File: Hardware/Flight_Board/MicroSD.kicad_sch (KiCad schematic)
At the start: 8 parts, among them J3 MEM2067-02-180-00-A_REVB

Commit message: clean up and finalize initial design
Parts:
- renumbered C19 to C25, C18 to C26, J3 to J5, R9 to R10, R7 to R11, R10 to R12, R6 to R9
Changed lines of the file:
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@@
   (symbol (lib_id "Device:R") (at 77.47 59.69 0) (unit 1)
     (in_bom yes) (on_board yes) (dnp no)
-    (property "Reference" "R10" (at 78.74 58.42 0)
+    (property "Reference" "R12" (at 78.74 58.42 0)
       (effects (font (size 1.27 1.27)) (justify left))
     )
@@
       (project "Flight_Board"
         (path "/e8eb85d5-f1ff-4500-895d-25b9ff5f6d36/d0c90712-c1df-4337-b369-5da6fbfa813f"
+          (reference "R12") (unit 1)
+        )
+      )
+    )
+  )
+  (symbol (lib_id "Device:R") (at 66.04 49.53 0) (unit 1)
+    (in_bom yes) (on_board yes) (dnp no)
+    (property "Reference" "R9" (at 67.31 48.26 0)
+      (effects (font (size 1.27 1.27)) (justify left))
+    )
+    (property "Value" "10k" (at 67.31 50.8 0)
+      (effects (font (size 1.27 1.27)) (justify left))
+    )
+    (property "Footprint" "" (at 64.262 49.53 90)
+      (effects (font (size 1.27 1.27)) hide)
+    )
+    (property "Datasheet" "~" (at 66.04 49.53 0)
+      (effects (font (size 1.27 1.27)) hide)
+    )
+    (pin "1")
+    (pin "2")
+    (instances
+      (project "Flight_Board"
+        (path "/e8eb85d5-f1ff-4500-895d-25b9ff5f6d36/d0c90712-c1df-4337-b369-5da6fbfa813f"
+          (reference "R9") (unit 1)
+        )
+      )
+    )
+  )
+  (symbol (lib_id "Device:R") (at 69.85 59.69 0) (unit 1)
+    (in_bom yes) (on_board yes) (dnp no)
+    (property "Reference" "R10" (at 71.12 58.42 0)
+      (effects (font (size 1.27 1.27)) (justify left))
+    )
+    (property "Value" "10k" (at 71.12 60.96 0)
+      (effects (font (size 1.27 1.27)) (justify left))
+    )
+    (property "Footprint" "" (at 68.072 59.69 90)
+      (effects (font (size 1.27 1.27)) hide)
+    )
+    (property "Datasheet" "~" (at 69.85 59.69 0)
+      (effects (font (size 1.27 1.27)) hide)
+    )
+    (pin "1")
+    (pin "2")
+    (instances
+      (project "Flight_Board"
+        (path "/e8eb85d5-f1ff-4500-895d-25b9ff5f6d36/d0c90712-c1df-4337-b369-5da6fbfa813f"
           (reference "R10") (unit 1)
         )
@@
     )
   )
-  (symbol (lib_id "Device:R") (at 66.04 49.53 0) (unit 1)
-    (in_bom yes) (on_board yes) (dnp no)
-    (property "Reference" "R6" (at 67.31 48.26 0)
-      (effects (font (size 1.27 1.27)) (justify left))
-    )
-    (property "Value" "10k" (at 67.31 50.8 0)
-      (effects (font (size 1.27 1.27)) (justify left))
-    )
-    (property "Footprint" "" (at 64.262 49.53 90)
-      (effects (font (size 1.27 1.27)) hide)
-    )
-    (property "Datasheet" "~" (at 66.04 49.53 0)
-      (effects (font (size 1.27 1.27)) hide)
-    )
-    (pin "1")
-    (pin "2")
-    (instances
-      (project "Flight_Board"
-        (path "/e8eb85d5-f1ff-4500-895d-25b9ff5f6d36/d0c90712-c1df-4337-b369-5da6fbfa813f"
-          (reference "R6") (unit 1)
-        )
-      )
-    )
-  )
-  (symbol (lib_id "Device:R") (at 69.85 59.69 0) (unit 1)
-    (in_bom yes) (on_board yes) (dnp no)
-    (property "Reference" "R9" (at 71.12 58.42 0)
-      (effects (font (size 1.27 1.27)) (justify left))
-    )
-    (property "Value" "10k" (at 71.12 60.96 0)
-      (effects (font (size 1.27 1.27)) (justify left))
-    )
-    (property "Footprint" "" (at 68.072 59.69 90)
-      (effects (font (size 1.27 1.27)) hide)
-    )
-    (property "Datasheet" "~" (at 69.85 59.69 0)
-      (effects (font (size 1.27 1.27)) hide)
-    )
-    (pin "1")
-    (pin "2")
-    (instances
-      (project "Flight_Board"
-        (path "/e8eb85d5-f1ff-4500-895d-25b9ff5f6d36/d0c90712-c1df-4337-b369-5da6fbfa813f"
-          (reference "R9") (unit 1)
-        )
-      )
-    )
-  )
   (symbol (lib_id "power:GND") (at 107.95 99.06 0) (unit 1)
     (in_bom yes) (on_board yes) (dnp no)
-    (property "Reference" "#PWR036" (at 107.95 105.41 0)
+    (property "Reference" "#PWR046" (at 107.95 105.41 0)
       (effects (font (size 1.27 1.27)) hide)
     )
@@
       (project "Flight_Board"
         (path "/e8eb85d5-f1ff-4500-895d-25b9ff5f6d36/d0c90712-c1df-4337-b369-5da6fbfa813f"
-          (reference "#PWR036") (unit 1)
+          (reference "#PWR046") (unit 1)
         )
       )
@@
   (symbol (lib_id "power:+3.3V") (at 88.9 41.91 0) (unit 1)
     (in_bom yes) (on_board yes) (dnp no) (fields_autoplaced)
-    (property "Reference" "#PWR035" (at 88.9 45.72 0)
+    (property "Reference" "#PWR043" (at 88.9 45.72 0)
       (effects (font (size 1.27 1.27)) hide)
     )
@@
       (project "Flight_Board"
         (path "/e8eb85d5-f1ff-4500-895d-25b9ff5f6d36/d0c90712-c1df-4337-b369-5da6fbfa813f"
-          (reference "#PWR035") (unit 1)
+          (reference "#PWR043") (unit 1)
         )
       )
@@
   (symbol (lib_id "Project:MEM2067-02-180-00-A_REVB") (at 115.57 76.2 0) (unit 1)
     (in_bom yes) (on_board yes) (dnp no) (fields_autoplaced)
-    (property "Reference" "J3" (at 132.08 80.01 0)
+    (property "Reference" "J5" (at 132.08 80.01 0)
       (effects (font (size 1.27 1.27)) (justify left))
     )
@@
       (project "Flight_Board"
         (path "/e8eb85d5-f1ff-4500-895d-25b9ff5f6d36/d0c90712-c1df-4337-b369-5da6fbfa813f"
-          (reference "J3") (unit 1)
+          (reference "J5") (unit 1)
         )
       )
@@
   (symbol (lib_id "Device:C") (at 99.06 45.72 0) (unit 1)
     (in_bom yes) (on_board yes) (dnp no)
-    (property "Reference" "C18" (at 101.6 44.45 0)
+    (property "Reference" "C26" (at 101.6 44.45 0)
       (effects (font (size 1.27 1.27)) (justify left))
     )
@@
       (project "Flight_Board"
         (path "/e8eb85d5-f1ff-4500-895d-25b9ff5f6d36/d0c90712-c1df-4337-b369-5da6fbfa813f"
-          (reference "C18") (unit 1)
+          (reference "C26") (unit 1)
         )
       )
@@
   (symbol (lib_id "power:GND") (at 99.06 49.53 0) (unit 1)
     (in_bom yes) (on_board yes) (dnp no)
-    (property "Reference" "#PWR037" (at 99.06 55.88 0)
+    (property "Reference" "#PWR045" (at 99.06 55.88 0)
       (effects (font (size 1.27 1.27)) hide)
     )
@@
       (project "Flight_Board"
         (path "/e8eb85d5-f1ff-4500-895d-25b9ff5f6d36/d0c90712-c1df-4337-b369-5da6fbfa813f"
-          (reference "#PWR037") (unit 1)
+          (reference "#PWR045") (unit 1)
         )
       )
@@
   (symbol (lib_id "Device:R") (at 73.66 49.53 0) (unit 1)
     (in_bom yes) (on_board yes) (dnp no)
-    (property "Reference" "R7" (at 74.93 48.26 0)
+    (property "Reference" "R11" (at 74.93 48.26 0)
       (effects (font (size 1.27 1.27)) (justify left))
     )
@@
       (project "Flight_Board"
         (path "/e8eb85d5-f1ff-4500-895d-25b9ff5f6d36/d0c90712-c1df-4337-b369-5da6fbfa813f"
-          (reference "R7") (unit 1)
+          (reference "R11") (unit 1)
         )
       )
@@
   (symbol (lib_id "power:GND") (at 88.9 49.53 0) (unit 1)
     (in_bom yes) (on_board yes) (dnp no)
-    (property "Reference" "#PWR038" (at 88.9 55.88 0)
+    (property "Reference" "#PWR044" (at 88.9 55.88 0)
       (effects (font (size 1.27 1.27)) hide)
     )
@@
       (project "Flight_Board"
         (path "/e8eb85d5-f1ff-4500-895d-25b9ff5f6d36/d0c90712-c1df-4337-b369-5da6fbfa813f"
-          (reference "#PWR038") (unit 1)
+          (reference "#PWR044") (unit 1)
         )
       )
@@
   (symbol (lib_id "Device:C") (at 88.9 45.72 0) (unit 1)
     (in_bom yes) (on_board yes) (dnp no)
-    (property "Reference" "C19" (at 91.44 44.45 0)
+    (property "Reference" "C25" (at 91.44 44.45 0)
       (effects (font (size 1.27 1.27)) (justify left))
     )
@@
       (project "Flight_Board"
         (path "/e8eb85d5-f1ff-4500-895d-25b9ff5f6d36/d0c90712-c1df-4337-b369-5da6fbfa813f"
-          (reference "C19") (unit 1)
-        )
-      )
+          (reference "C25") (unit 1)
+        )
+      )

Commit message: Added Mason's Feedback
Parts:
- added C33, C34, C35, C36: 22p, symbol Device:C
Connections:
- net GND: now also C33.2, C34.2, C35.2, C36.2
- net SDIO_D0: now also C36.1
- net SDIO_D1: now also C35.1
- net SDIO_D2: now also C34.1
- net SDIO_D3: now also C33.1
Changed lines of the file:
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@@
   (junction (at 99.06 41.91) (diameter 0) (color 0 0 0 0)
   )
-  (wire (pts (xy 110.49 76.2) (xy 66.04 76.2))
+  (wire (pts (xy 66.04 76.2) (xy 110.49 76.2))
     (stroke (width 0) (type default))
   )
@@
     (stroke (width 0) (type default))
   )
-  (wire (pts (xy 110.49 68.58) (xy 77.47 68.58))
+  (wire (pts (xy 73.66 71.12) (xy 73.66 82.55))
+    (stroke (width 0) (type default))
+  )
+  (wire (pts (xy 77.47 68.58) (xy 110.49 68.58))
     (stroke (width 0) (type default))
   )
@@
     (stroke (width 0) (type default))
   )
-  (wire (pts (xy 77.47 68.58) (xy 77.47 63.5))
-    (stroke (width 0) (type default))
-  )
   (wire (pts (xy 110.49 66.04) (xy 107.95 66.04))
     (stroke (width 0) (type default))
@@
     (stroke (width 0) (type default))
   )
+  (wire (pts (xy 77.47 68.58) (xy 77.47 86.36))
+    (stroke (width 0) (type default))
+  )
   (wire (pts (xy 110.49 88.9) (xy 107.95 88.9))
     (stroke (width 0) (type default))
@@
     (stroke (width 0) (type default))
   )
+  (wire (pts (xy 69.85 73.66) (xy 69.85 92.71))
+    (stroke (width 0) (type default))
+  )
   (wire (pts (xy 107.95 41.91) (xy 107.95 66.04))
     (stroke (width 0) (type default))
@@
     (stroke (width 0) (type default))
   )
+  (wire (pts (xy 66.04 76.2) (xy 66.04 86.36))
+    (stroke (width 0) (type default))
+  )
   (wire (pts (xy 107.95 96.52) (xy 107.95 99.06))
     (stroke (width 0) (type default))
@@
   )
   (wire (pts (xy 77.47 41.91) (xy 77.47 55.88))
+    (stroke (width 0) (type default))
+  )
+  (wire (pts (xy 77.47 63.5) (xy 77.47 68.58))
     (stroke (width 0) (type default))
   )
@@
         (path "/e8eb85d5-f1ff-4500-895d-25b9ff5f6d36/d0c90712-c1df-4337-b369-5da6fbfa813f"
           (reference "#PWR043") (unit 1)
+        )
+      )
+    )
+  )
+  (symbol (lib_id "Device:C") (at 73.66 86.36 0) (unit 1)
+    (in_bom yes) (on_board yes) (dnp no)
+    (property "Reference" "C35" (at 76.2 82.55 0)
+      (effects (font (size 1.27 1.27)) (justify left))
+    )
+    (property "Value" "22p" (at 77.47 85.09 0)
+      (effects (font (size 1.27 1.27)) (justify left))
+    )
+    (property "Footprint" "" (at 74.6252 90.17 0)
+      (effects (font (size 1.27 1.27)) hide)
+    )
+    (property "Datasheet" "~" (at 73.66 86.36 0)
+      (effects (font (size 1.27 1.27)) hide)
+    )
+    (pin "1")
+    (pin "2")
+    (instances
+      (project "Flight_Board"
+        (path "/e8eb85d5-f1ff-4500-895d-25b9ff5f6d36/d0c90712-c1df-4337-b369-5da6fbfa813f"
+          (reference "C35") (unit 1)
         )
       )
@@
     )
   )
+  (symbol (lib_id "power:GND") (at 77.47 93.98 0) (unit 1)
+    (in_bom yes) (on_board yes) (dnp no)
+    (property "Reference" "#PWR064" (at 77.47 100.33 0)
+      (effects (font (size 1.27 1.27)) hide)
+    )
+    (property "Value" "GND" (at 77.47 97.79 0)
+      (effects (font (size 1.27 1.27)))
+    )
+    (property "Footprint" "" (at 77.47 93.98 0)
+      (effects (font (size 1.27 1.27)) hide)
+    )
+    (property "Datasheet" "" (at 77.47 93.98 0)
+      (effects (font (size 1.27 1.27)) hide)
+    )
+    (pin "1")
+    (instances
+      (project "Flight_Board"
+        (path "/e8eb85d5-f1ff-4500-895d-25b9ff5f6d36/d0c90712-c1df-4337-b369-5da6fbfa813f"
+          (reference "#PWR064") (unit 1)
+        )
+      )
+    )
+  )
   (symbol (lib_id "power:GND") (at 99.06 49.53 0) (unit 1)
     (in_bom yes) (on_board yes) (dnp no)
@@
     )
   )
+  (symbol (lib_id "Device:C") (at 69.85 96.52 0) (unit 1)
+    (in_bom yes) (on_board yes) (dnp no)
+    (property "Reference" "C34" (at 71.12 97.79 0)
+      (effects (font (size 1.27 1.27)) (justify left))
+    )
+    (property "Value" "22p" (at 71.12 100.33 0)
+      (effects (font (size 1.27 1.27)) (justify left))
+    )
+    (property "Footprint" "" (at 70.8152 100.33 0)
+      (effects (font (size 1.27 1.27)) hide)
+    )
+    (property "Datasheet" "~" (at 69.85 96.52 0)
+      (effects (font (size 1.27 1.27)) hide)
+    )
+    (pin "1")
+    (pin "2")
+    (instances
+      (project "Flight_Board"
+        (path "/e8eb85d5-f1ff-4500-895d-25b9ff5f6d36/d0c90712-c1df-4337-b369-5da6fbfa813f"
+          (reference "C34") (unit 1)
+        )
+      )
+    )
+  )
+  (symbol (lib_id "Device:C") (at 77.47 90.17 0) (unit 1)
+    (in_bom yes) (on_board yes) (dnp no)
+    (property "Reference" "C36" (at 80.01 88.9 0)
+      (effects (font (size 1.27 1.27)) (justify left))
+    )
+    (property "Value" "22p" (at 80.01 91.44 0)
+      (effects (font (size 1.27 1.27)) (justify left))
+    )
+    (property "Footprint" "" (at 78.4352 93.98 0)
+      (effects (font (size 1.27 1.27)) hide)
+    )
+    (property "Datasheet" "~" (at 77.47 90.17 0)
+      (effects (font (size 1.27 1.27)) hide)
+    )
+    (pin "1")
+    (pin "2")
+    (instances
+      (project "Flight_Board"
+        (path "/e8eb85d5-f1ff-4500-895d-25b9ff5f6d36/d0c90712-c1df-4337-b369-5da6fbfa813f"
+          (reference "C36") (unit 1)
+        )
+      )
+    )
+  )
+  (symbol (lib_id "power:GND") (at 66.04 93.98 0) (unit 1)
+    (in_bom yes) (on_board yes) (dnp no)
+    (property "Reference" "#PWR062" (at 66.04 100.33 0)
+      (effects (font (size 1.27 1.27)) hide)
+    )
+    (property "Value" "GND" (at 66.04 97.79 0)
+      (effects (font (size 1.27 1.27)))
+    )
+    (property "Footprint" "" (at 66.04 93.98 0)
+      (effects (font (size 1.27 1.27)) hide)
+    )
+    (property "Datasheet" "" (at 66.04 93.98 0)
+      (effects (font (size 1.27 1.27)) hide)
+    )
+    (pin "1")
+    (instances
+      (project "Flight_Board"
+        (path "/e8eb85d5-f1ff-4500-895d-25b9ff5f6d36/d0c90712-c1df-4337-b369-5da6fbfa813f"
+          (reference "#PWR062") (unit 1)
+        )
+      )
+    )
+  )
   (symbol (lib_id "power:GND") (at 88.9 49.53 0) (unit 1)
     (in_bom yes) (on_board yes) (dnp no)
@@
     )
   )
+  (symbol (lib_id "Device:C") (at 66.04 90.17 0) (unit 1)
+    (in_bom yes) (on_board yes) (dnp no)
+    (property "Reference" "C33" (at 68.58 88.9 0)
+      (effects (font (size 1.27 1.27)) (justify left))
+    )
+    (property "Value" "22p" (at 68.58 91.44 0)
+      (effects (font (size 1.27 1.27)) (justify left))
+    )
+    (property "Footprint" "" (at 67.0052 93.98 0)
+      (effects (font (size 1.27 1.27)) hide)
+    )
+    (property "Datasheet" "~" (at 66.04 90.17 0)
+      (effects (font (size 1.27 1.27)) hide)
+    )
+    (pin "1")
+    (pin "2")
+    (instances
+      (project "Flight_Board"
+        (path "/e8eb85d5-f1ff-4500-895d-25b9ff5f6d36/d0c90712-c1df-4337-b369-5da6fbfa813f"
+          (reference "C33") (unit 1)
+        )
+      )
+    )
+  )
   (symbol (lib_id "Device:C") (at 88.9 45.72 0) (unit 1)
     (in_bom yes) (on_board yes) (dnp no)
@@
     )
   )
+  (symbol (lib_id "power:GND") (at 73.66 90.17 0) (unit 1)
+    (in_bom yes) (on_board yes) (dnp no)
+    (property "Reference" "#PWR065" (at 73.66 96.52 0)
+      (effects (font (size 1.27 1.27)) hide)
+    )
+    (property "Value" "GND" (at 73.66 93.98 0)
+      (effects (font (size 1.27 1.27)))
+    )
+    (property "Footprint" "" (at 73.66 90.17 0)
+      (effects (font (size 1.27 1.27)) hide)
+    )
+    (property "Datasheet" "" (at 73.66 90.17 0)
+      (effects (font (size 1.27 1.27)) hide)
+    )
+    (pin "1")
+    (instances
+      (project "Flight_Board"
+        (path "/e8eb85d5-f1ff-4500-895d-25b9ff5f6d36/d0c90712-c1df-4337-b369-5da6fbfa813f"
+          (reference "#PWR065") (unit 1)
+        )
+      )
+    )
+  )
   (symbol (lib_id "Device:R") (at 62.23 59.69 0) (unit 1)
     (in_bom yes) (on_board yes) (dnp no)
@@
         )
       )
+    )
+  )
+  (symbol (lib_id "power:GND") (at 69.85 100.33 0) (unit 1)
+    (in_bom yes) (on_board yes) (dnp no)
+    (property "Reference" "#PWR063" (at 69.85 106.68 0)
+      (effects (font (size 1.27 1.27)) hide)
+    )
+    (property "Value" "GND" (at 69.85 104.14 0)
+      (effects (font (size 1.27 1.27)))
+    )
+    (property "Footprint" "" (at 69.85 100.33 0)
+      (effects (font (size 1.27 1.27)) hide)
+    )
+    (property "Datasheet" "" (at 69.85 100.33 0)
+      (effects (font (size 1.27 1.27)) hide)
+    )
+    (pin "1")
+    (instances
+      (project "Flight_Board"
+        (path "/e8eb85d5-f1ff-4500-895d-25b9ff5f6d36/d0c90712-c1df-4337-b369-5da6fbfa813f"
+          (reference "#PWR063") (unit 1)
+        )
+      )

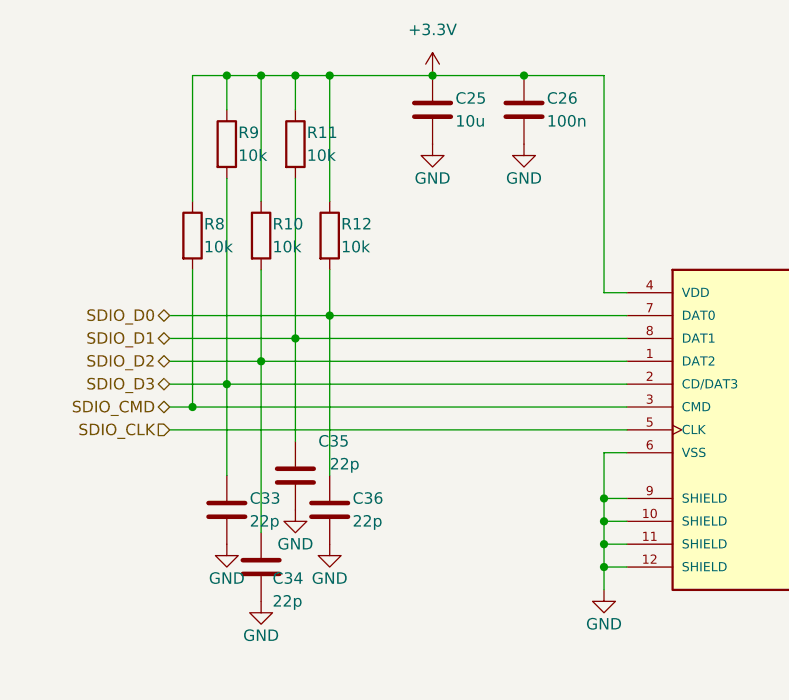
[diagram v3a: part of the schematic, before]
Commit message: Clean up, relabel all refdes, and add autosaved files to gitignore
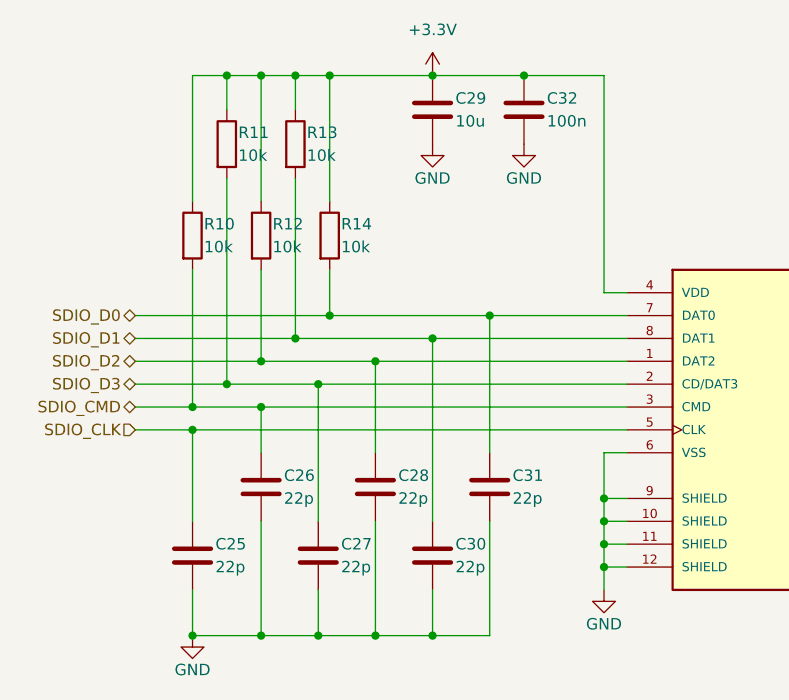
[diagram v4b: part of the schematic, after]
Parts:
- removed C33, C34, C35: 22p, symbol Device:C
- added C25, C26, C27, C28, C30: 22p, symbol Device:C
- renumbered C25 to C29, C36 to C31, C26 to C32, R8 to R10, R9 to R11, R10 to R12, R11 to R13, R12 to R14
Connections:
- net GND: now also C25.2, C26.2, C27.2, C28.2, C30.2
- net SDIO_CLK: now also C25.1
- net SDIO_CMD: now also C26.1
- net SDIO_D1: now also C30.1
- net SDIO_D2: now also C28.1
- net SDIO_D3: now also C27.1
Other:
- moved on the sheet: C31
